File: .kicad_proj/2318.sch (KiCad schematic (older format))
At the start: 2 parts, among them J1 Micro_SD_Card, U1 ATmega328-PU

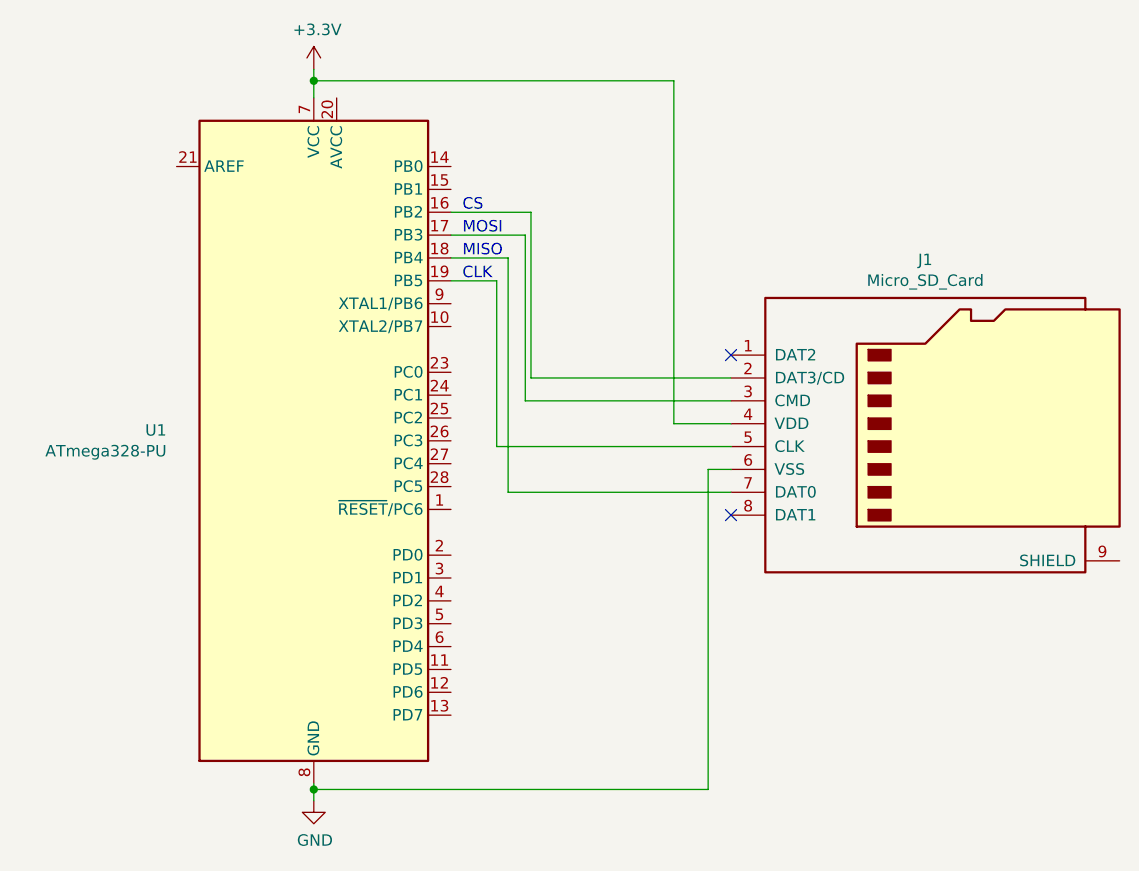
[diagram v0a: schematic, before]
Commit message: Add resistors
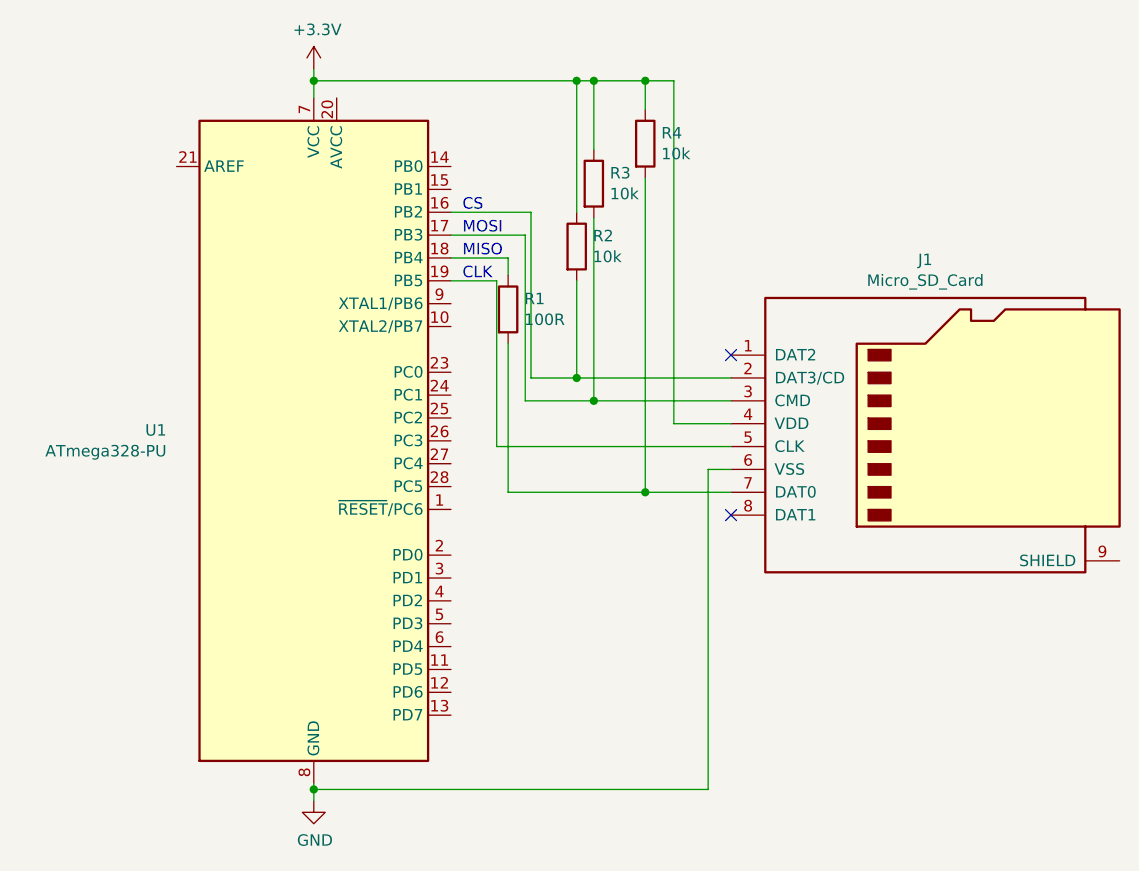
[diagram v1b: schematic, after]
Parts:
- added R1: 100R, symbol Device:R
- added R2, R3, R4: 10k, symbol Device:R
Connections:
- net +3V3: now also R2.1, R3.1, R4.1
- net at J1.2 (DAT3/CD), U1.16 (PB2): now also R2.2
- net at J1.3 (CMD), U1.17 (PB3): now also R3.2
- net at U1.18 (PB4): now also R1.1; no longer J1.7 (DAT0)
- new net: J1.7 (DAT0), R1.2, R4.2
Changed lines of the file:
@@
 $EndComp
-Wire Wire Line
-	6775 3225 5900 3225
 Wire Wire Line
 	5900 3225 5900 2500
@@
 	5875 2600 5875 3325
 Wire Wire Line
-	5875 3325 6775 3325
+	5875 3325 6175 3325
 Wire Wire Line
-	6775 3725 5800 3725
-Wire Wire Line
-	5800 3725 5800 2700
+	6775 3725 6400 3725
 Wire Wire Line
 	5800 2700 5550 2700
 Wire Wire Line
-	4950 1925 6525 1925
+	4950 1925 6100 1925
 NoConn ~ 6775 3125
 NoConn ~ 6775 3825
+$Comp
+L Device:R R1
+U 1 1 60D4D984
+P 5800 2925
+F 0 "R1" H 5870 2971 50  0000 L CNN
+F 1 "100R" H 5870 2880 50  0000 L CNN
+F 2 "" V 5730 2925 50  0001 C CNN
+F 3 "~" H 5800 2925 50  0001 C CNN
+	1    5800 2925
+	1    0    0    -1
+$EndComp
+Wire Wire Line
+	5800 2775 5800 2700
+Wire Wire Line
+	5800 3075 5800 3725
+$Comp
+L Device:R R2
+U 1 1 60D4DAD7
+P 6100 2650
+F 0 "R2" H 6170 2696 50  0000 L CNN
+F 1 "10k" H 6170 2605 50  0000 L CNN
+F 2 "" V 6030 2650 50  0001 C CNN
+F 3 "~" H 6100 2650 50  0001 C CNN
+	1    6100 2650
+	1    0    0    -1
+$EndComp
+$Comp
+L Device:R R3
+U 1 1 60D4EBE4
+P 6175 2375
+F 0 "R3" H 6245 2421 50  0000 L CNN
+F 1 "10k" H 6245 2330 50  0000 L CNN
+F 2 "" V 6105 2375 50  0001 C CNN
+F 3 "~" H 6175 2375 50  0001 C CNN
+	1    6175 2375
+	1    0    0    -1
+$EndComp
+Wire Wire Line
+	6100 2800 6100 3225
+Wire Wire Line
+	5900 3225 6100 3225
+Connection ~ 6100 3225
+Wire Wire Line
+	6100 3225 6775 3225
+Wire Wire Line
+	6175 2525 6175 3325
+Connection ~ 6175 3325
+Wire Wire Line
+	6175 3325 6775 3325
+$Comp
+L Device:R R4
+U 1 1 60D5059D
+P 6400 2200
+F 0 "R4" H 6470 2246 50  0000 L CNN
+F 1 "10k" H 6470 2155 50  0000 L CNN
+F 2 "" V 6330 2200 50  0001 C CNN
+F 3 "~" H 6400 2200 50  0001 C CNN
+	1    6400 2200
+	1    0    0    -1
+$EndComp
+Wire Wire Line
+	6100 2500 6100 1925
+Connection ~ 6100 1925
+Wire Wire Line
+	6100 1925 6175 1925
+Wire Wire Line
+	6175 2225 6175 1925
+Connection ~ 6175 1925
+Wire Wire Line
+	6175 1925 6400 1925
+Wire Wire Line
+	6400 2050 6400 1925
+Connection ~ 6400 1925
+Wire Wire Line
+	6400 1925 6525 1925
+Wire Wire Line
+	6400 2350 6400 3725
+Connection ~ 6400 3725
+Wire Wire Line
+	6400 3725 5800 3725
 $EndSCHEMATC
